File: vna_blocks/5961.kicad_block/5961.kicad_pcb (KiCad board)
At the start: 4 copper layers, 23 parts, among them U10 ADL5961ACCZ

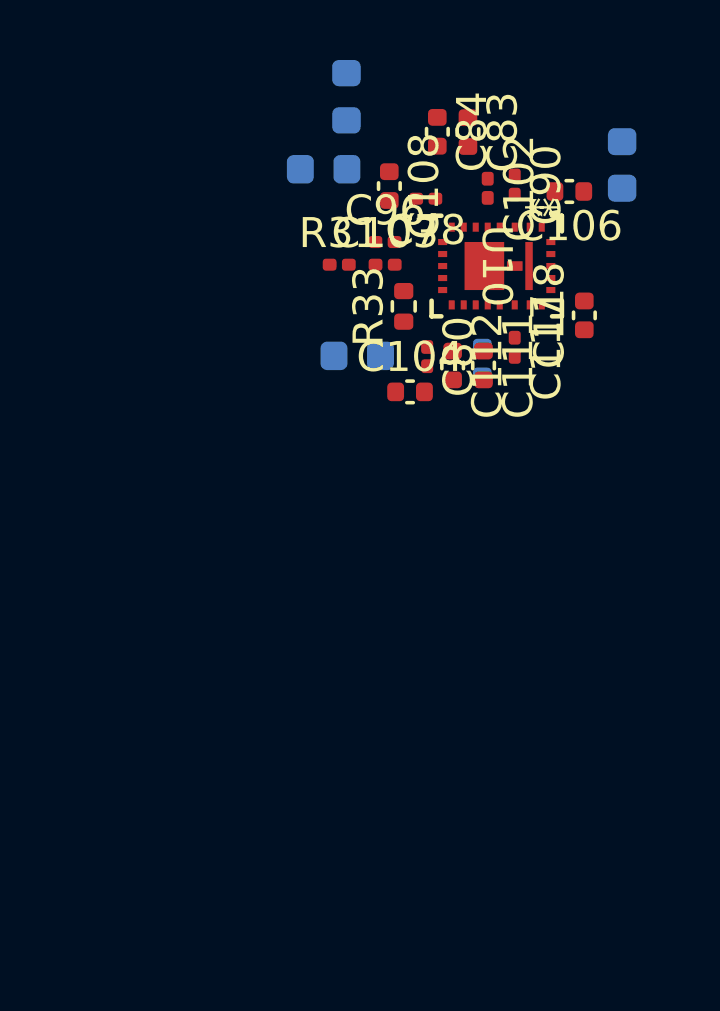
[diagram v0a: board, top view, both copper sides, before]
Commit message: new parts, design blocks updated
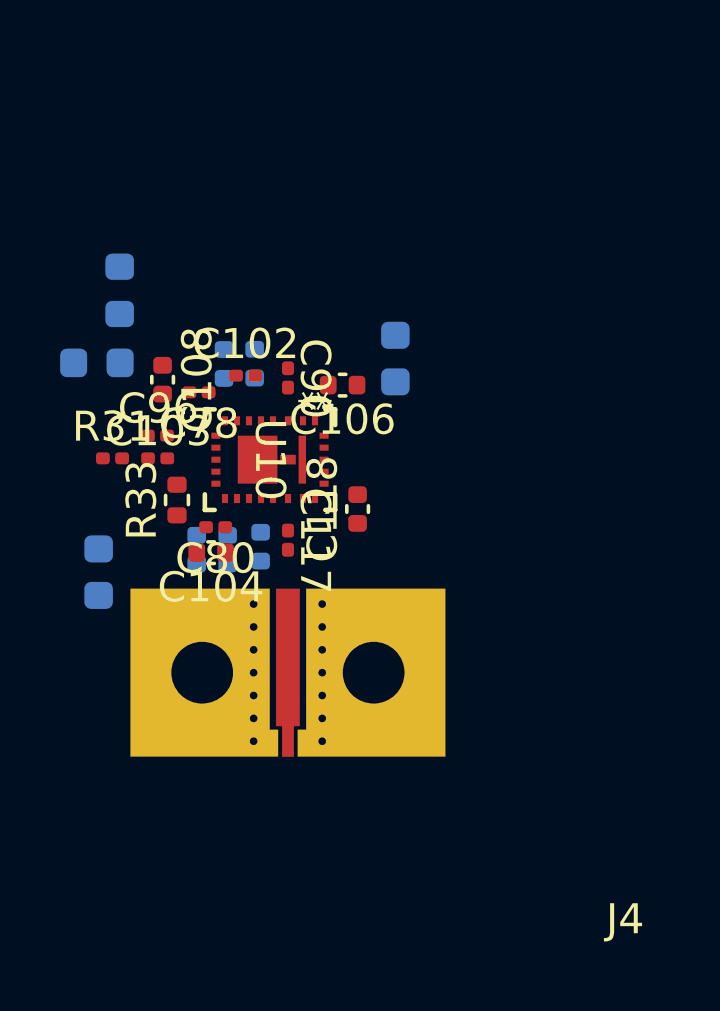
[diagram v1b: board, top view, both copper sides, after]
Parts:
- added J4: DUT_Port_2, VNA_fp:AMPHENOL_2921-61674, F.Cu at (212.9, 161.1)
- C103, C117, C90, C96: footprint Capacitor_SMD:C_0201_0603Metric -> VNA_fp:P21BN
- C111, C112, C83, C84: moved to B.Cu
- moved C87 11.2 mm to (206.6, 157.8), turned to -90 degrees
- moved C111 10.5 mm to (210.9, 157.0), turned to 90 degrees
- moved C112 10.5 mm to (209.9, 157.0), turned to 90 degrees
- moved C84 10.5 mm to (210.8, 150.8), turned to 90 degrees
- moved C83 10.5 mm to (211.8, 150.8), turned to 90 degrees
- moved C102 10.2 mm to (211.5, 151.2), turned to 0 degrees
- moved R33 9.94 mm to (209.2, 155.3)
- moved C105 9.94 mm to (216.5, 150.6)
- moved C96 9.94 mm to (208.6, 153.2)
- moved FB2 9.94 mm to (207.3, 148.4)
- moved C103 9.94 mm to (208.6, 154.0)
- moved C106 9.94 mm to (214.7, 151.5)
- moved C108 9.94 mm to (208.7, 151.3)
- moved C117 9.94 mm to (212.9, 156.7)
- moved C118 9.94 mm to (215.2, 155.6)
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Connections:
- net /Front_end_receiver/IF1R_N renamed /Front_end_receiver/IF2R_N
- net /Front_end_receiver/IF1R_P renamed /Front_end_receiver/IF2R_P
- net Net-(U10-OFM) renamed /f_OF2_N
- net Net-(U10-OFP) renamed /f_OF2_P

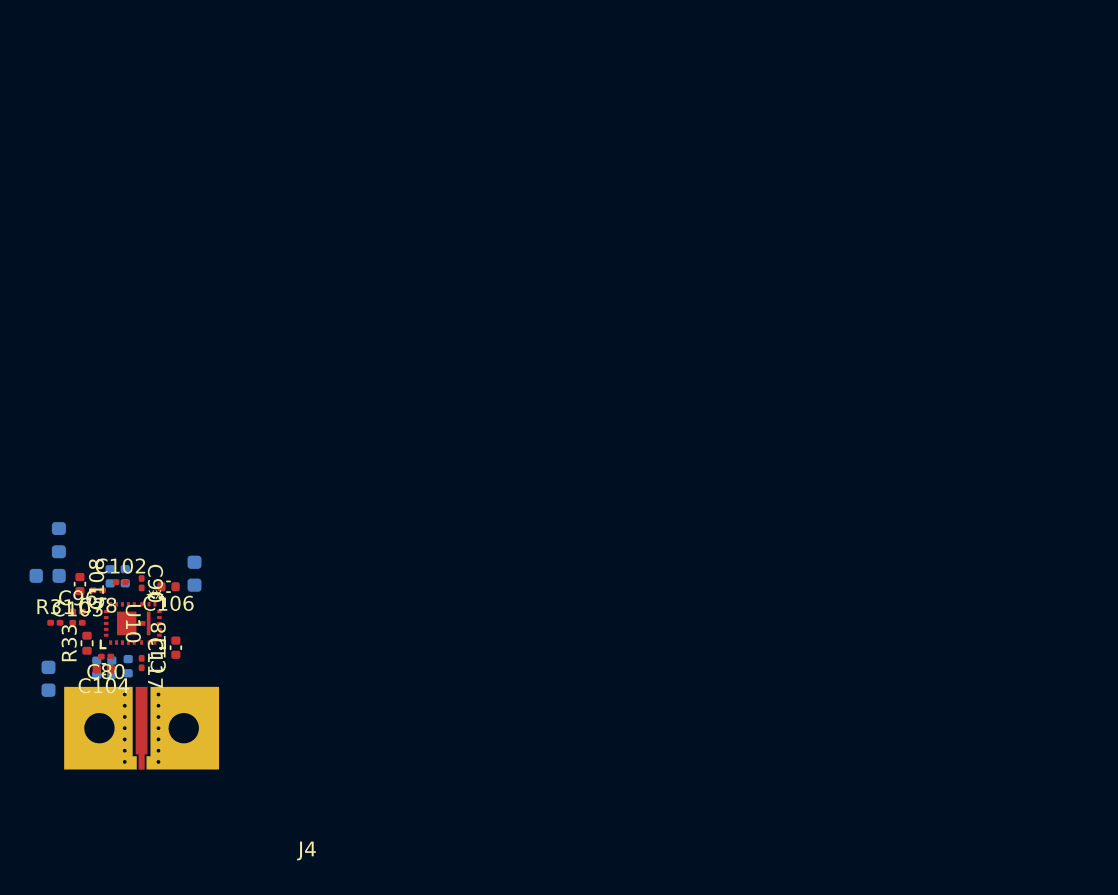
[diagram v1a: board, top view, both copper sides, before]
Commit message: fixed 50 ohm for coax port, fixed power blocks
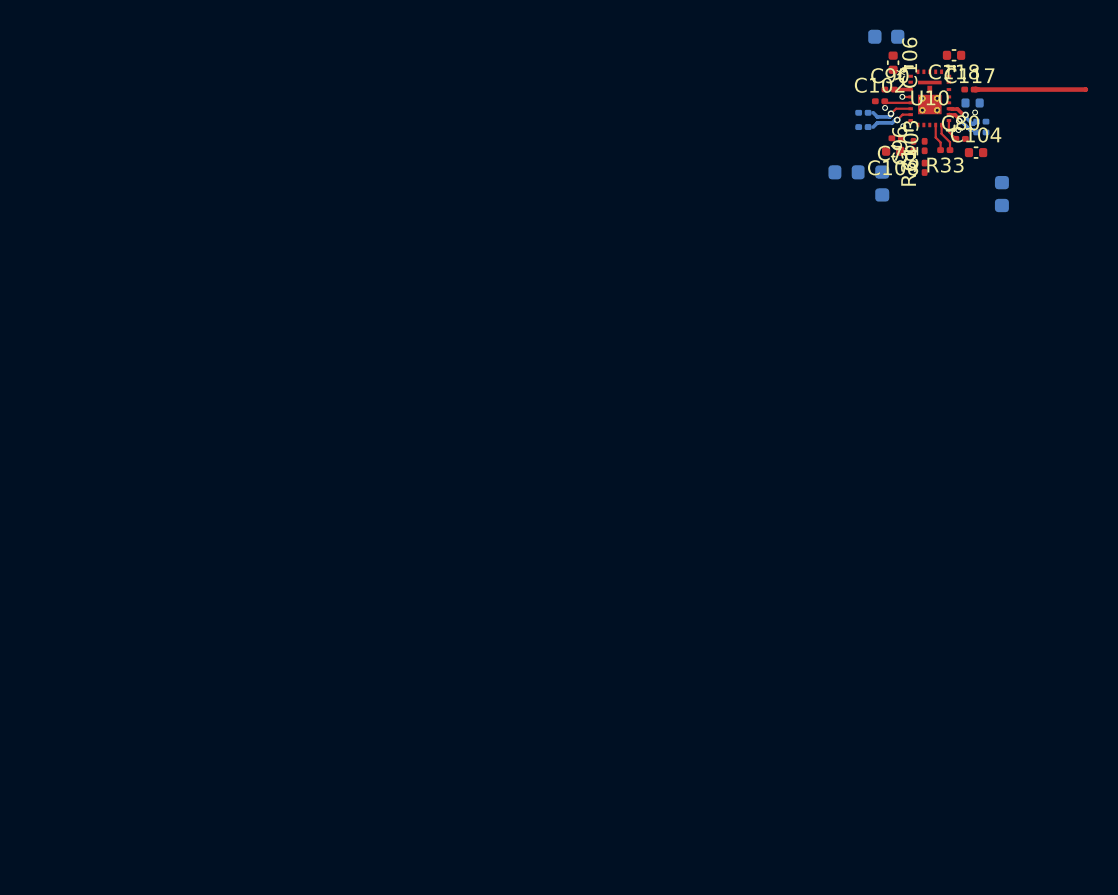
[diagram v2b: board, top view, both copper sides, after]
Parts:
- removed J4: DUT_Port_2, VNA_fp:AMPHENOL_2921-61674
- C111, C112, C83, C84: footprint Capacitor_SMD:C_0402_1005Metric -> Capacitor_SMD:C_0201_0603Metric
- R33: footprint Resistor_SMD:R_0402_1005Metric -> Resistor_SMD:R_0201_0603Metric
- moved C87 72.5 mm to (271.2, 124.9)
- moved C112 70.1 mm to (269.8, 120.7), turned to 0 degrees
- moved C111 69.6 mm to (269.8, 120.0), turned to 0 degrees
- moved C116 68.8 mm to (269.2, 118.7), turned to 180 degrees
- moved C104 68.7 mm to (269.5, 122.1), turned to 0 degrees
- moved C117 68.3 mm to (269.0, 117.8), turned to 0 degrees
- moved C80 67.7 mm to (268.4, 121.2), turned to 0 degrees
- moved R33 67.1 mm to (267.4, 121.9), turned to 180 degrees
- moved R31 66.5 mm to (266.0, 123.1), turned to 90 degrees
- moved C118 66.3 mm to (268.0, 115.5), turned to 180 degrees
- moved C103 65.9 mm to (266.0, 121.6), turned to 90 degrees
- moved C96 64.8 mm to (265.2, 121.6), turned to 90 degrees
- moved U10 64.7 mm to (266.3, 118.4), turned to 0 degrees
- moved C93 62.5 mm to (263.1, 124.2), turned to -90 degrees
- moved C108 62.4 mm to (263.8, 122.0), turned to 180 degrees
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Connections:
- net /1V8D renamed /1V8_IO
- net Net-(U10-IFFM) renamed /Front_end_receiver/2_6_N
- net Net-(U10-IFFP) renamed /Front_end_receiver/2_6_P
- net Net-(U10-IFRM) renamed /Front_end_receiver/2_15_N
- net Net-(U10-IFRP) renamed /Front_end_receiver/2_15_P
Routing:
- net /DUT_P2: track 0.00 -> 7.57 mm
- net /Front_end_receiver/2_6_N: track 0.00 -> 2.97 mm, vias 0 -> 1
- net /Front_end_receiver/2_6_P: track 0.00 -> 2.89 mm, vias 0 -> 1
- net /Front_end_receiver/2_15_N: track 0.00 -> 2.46 mm, vias 0 -> 1
- net /Front_end_receiver/2_15_P: track 0.00 -> 2.46 mm, vias 0 -> 1
- net /f_OF2_N: track 0.00 -> 1.94 mm
- net /f_OF2_P: track 0.00 -> 1.84 mm
- net Net-(U10-CAP): track 0.00 -> 1.80 mm
- net /Front_end_receiver/5V_RCVR2_OVCC: track 0.00 -> 1.44 mm
- net Net-(U10-RFIN): track 0.00 -> 1.11 mm
- net GNDA: track 0.00 -> 0.57 mm, vias 0 -> 5
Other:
- copper layers 4 -> 8
